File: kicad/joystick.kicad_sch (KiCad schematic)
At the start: 5 parts, among them J3501 Conn_01x10, J3502 Conn_01x10

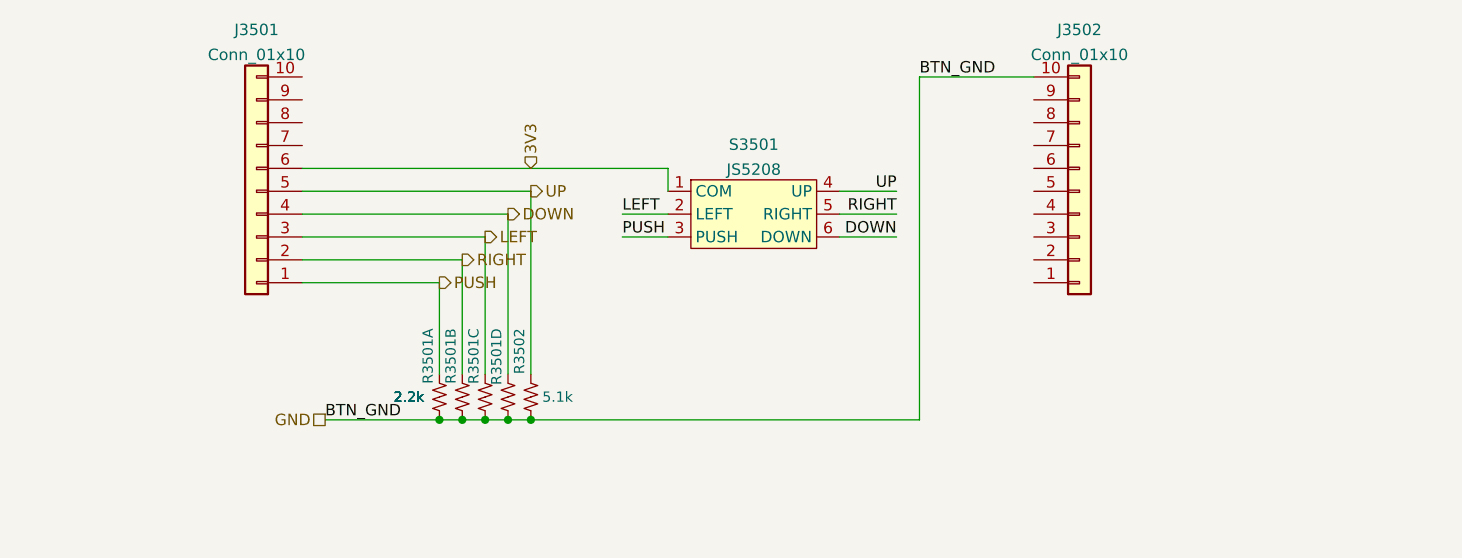
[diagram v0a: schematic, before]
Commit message: Replaced JS5208 with smaller JS1400
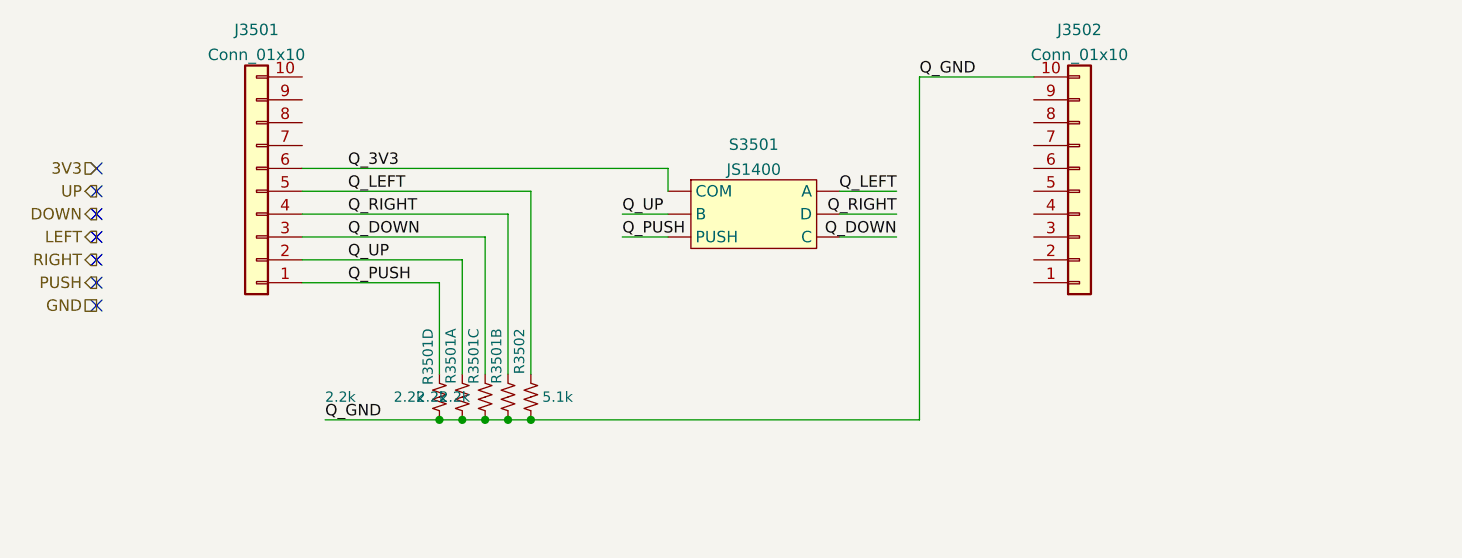
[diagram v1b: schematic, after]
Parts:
- S3501: value JS5208 -> JS1400; footprint KwanSystems:JS5208 -> KwanSystems:JS1400
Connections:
- net 3V3: no longer J3501.6 (Pin_6), S3501.1 (COM)
- net DOWN: no longer J3501.4 (Pin_4), R3501.5, S3501.6 (DOWN)
- net GND: no longer J3502.10 (Pin_10), R3501.1 (4), R3501.2 (4), R3501.3 (4), R3501.4, R3502.1
- net LEFT: no longer J3501.3 (Pin_3), R3501.6 (5), S3501.2 (LEFT)
- net PUSH: no longer J3501.1 (Pin_1), R3501.8 (5), S3501.3 (PUSH)
- net RIGHT: no longer J3501.2 (Pin_2), R3501.7 (5), S3501.5 (RIGHT)
- net UP: no longer J3501.5 (Pin_5), R3502.2, S3501.4 (UP)
- new net Q_3V3: J3501.6 (Pin_6), S3501.COM
- new net Q_DOWN: J3501.3 (Pin_3), R3501.6 (5), S3501.C
- new net Q_GND: J3502.10 (Pin_10), R3501.1 (4), R3501.2 (4), R3501.3 (4), R3501.4, R3502.1
- new net Q_LEFT: J3501.5 (Pin_5), R3502.2, S3501.A
- new net Q_PUSH: J3501.1 (Pin_1), R3501.5, S3501.PUSH
- new net Q_RIGHT: J3501.4 (Pin_4), R3501.7 (5), S3501.D
- new net Q_UP: J3501.2 (Pin_2), R3501.8 (5), S3501.B
- no-connect marks 0 -> 7
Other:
- moved on the sheet: R3501A, R3501B, R3501D

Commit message: Added graphical components to schematic for joystick board
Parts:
- added G3502: KwanSystems, KwanSystems:StKwansSoldermask, symbol KwanSystems:KwanSystems
- added G3503: DesignedWithKicad, KwanSystems:Symbol_KiCAD-Logo_CopperAndSilkScreenTop_small, symbol KwanSystems:DesignedWithKicad
- added G3504: OSHW, KwanSystems:OSHW-Symbol_6.7x6mm_SolderMask, symbol KwanSystems:OSHW
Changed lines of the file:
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@@
     (pin "8")
+  )
+  (symbol (lib_id "KwanSystems:OSHW") (at 222.885 161.925 0) (unit 1)
+    (in_bom no) (on_board yes)
+    (property "Reference" "G3504" (id 0) (at 234.315 161.925 0)
+      (effects (font (size 1.524 1.524)))
+    )
+    (property "Value" "OSHW" (id 1) (at 220.345 154.305 0)
+      (effects (font (size 1.524 1.524)) (justify left) hide)
+    )
+    (property "Footprint" "KwanSystems:OSHW-Symbol_6.7x6mm_SolderMask" (id 2) (at 222.885 161.925 0)
+      (effects (font (size 1.524 1.524)) hide)
+    )
+    (property "Datasheet" "" (id 3) (at 222.885 161.925 0)
+      (effects (font (size 1.524 1.524)) hide)
+    )
   )
   (symbol (lib_id "KwanSystems:RP4") (at 132.08 149.86 90) (unit 3)
@@
     (pin "3")
     (pin "6")
+  )
+  (symbol (lib_id "KwanSystems:DesignedWithKicad") (at 224.155 154.305 0) (unit 1)
+    (in_bom no) (on_board yes)
+    (property "Reference" "G3503" (id 0) (at 234.315 153.035 0)
+      (effects (font (size 1.524 1.524)))
+    )
+    (property "Value" "DesignedWithKicad" (id 1) (at 225.425 154.305 0)
+      (effects (font (size 1.524 1.524)) (justify left) hide)
+    )
+    (property "Footprint" "KwanSystems:Symbol_KiCAD-Logo_CopperAndSilkScreenTop_small" (id 2) (at 224.155 154.305 0)
+      (effects (font (size 1.524 1.524)) hide)
+    )
+    (property "Datasheet" "" (id 3) (at 224.155 154.305 0)
+      (effects (font (size 1.524 1.524)) hide)
+    )
   )
   (symbol (lib_id "KwanSystems:RESISTOR") (at 137.16 149.86 90) (unit 1)
@@
     (pin "7")
   )
+  (symbol (lib_id "KwanSystems:KwanSystems") (at 206.375 153.035 0) (unit 1)
+    (in_bom no) (on_board yes)
+    (property "Reference" "G3502" (id 0) (at 213.995 153.035 0)
+      (effects (font (size 1.524 1.524)))
+    )
+    (property "Value" "KwanSystems" (id 1) (at 211.455 153.035 0)
+      (effects (font (size 1.524 1.524)) (justify left) hide)
+    )
+    (property "Footprint" "KwanSystems:StKwansSoldermask" (id 2) (at 206.375 153.035 0)
+      (effects (font (size 1.524 1.524)) hide)
+    )
+    (property "Datasheet" "" (id 3) (at 206.375 153.035 0)
+      (effects (font (size 1.524 1.524)) hide)
+    )
+  )
   (symbol (lib_id "Connector_Generic:Conn_01x10") (at 106.68 127 180) (unit 1)

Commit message: Checkin before branch
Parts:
- S3501: value JS1400 -> JS5208; footprint KwanSystems:JS1400 -> KwanSystems:JS5208; Digikey EG4561-ND -> (none); Purpose Joystick -> (none)
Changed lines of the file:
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@@
     (pin "8")
+  )
+  (symbol (lib_id "KwanSystems:JS5208") (at 162.56 129.54 0) (unit 1)
+    (in_bom yes) (on_board yes) (fields_autoplaced)
+    (property "Reference" "S3501" (id 0) (at 161.925 122.081 0))
+    (property "Value" "JS5208" (id 1) (at 161.925 124.6179 0))
+    (property "Footprint" "KwanSystems:JS5208" (id 2) (at 162.56 129.54 0)
+      (effects (font (size 1.27 1.27)) hide)
+    )
+    (property "Datasheet" "" (id 3) (at 162.56 129.54 0)
+      (effects (font (size 1.27 1.27)) hide)
+    )
+    (pin "A")
+    (pin "B")
+    (pin "C")
+    (pin "COM")
+    (pin "D")
+    (pin "PUSH")
   )
   (symbol (lib_id "KwanSystems:OSHW") (at 222.885 161.925 0) (unit 1)
@@
     (pin "9")
   )
-  (symbol (lib_id "KwanSystems:JS5208") (at 162.56 129.54 0) (unit 1)
-    (in_bom yes) (on_board yes) (fields_autoplaced)
-    (property "Reference" "S3501" (id 0) (at 161.925 121.8143 0))
-    (property "Value" "JS1400" (id 1) (at 161.925 124.5894 0))
-    (property "Footprint" "KwanSystems:JS1400" (id 2) (at 162.56 129.54 0)
-      (effects (font (size 1.27 1.27)) hide)
-    )
-    (property "Datasheet" "" (id 3) (at 162.56 129.54 0)
-      (effects (font (size 1.27 1.27)) hide)
-    )
-    (property "Digikey" "EG4561-ND" (id 4) (at 162.56 129.54 0)
-      (effects (font (size 1.27 1.27)) hide)
-    )
-    (property "Purpose" "Joystick" (id 5) (at 162.56 129.54 0)
-      (effects (font (size 1.27 1.27)) hide)
-    )
-    (pin "A")
-    (pin "B")
-    (pin "C")
-    (pin "COM")
-    (pin "D")
-    (pin "PUSH")
-  )
 )
